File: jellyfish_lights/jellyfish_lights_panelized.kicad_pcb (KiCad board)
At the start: 2 copper layers, 162.8 x 143.6 mm, 424 parts, among them Q1 AO3400A, SW1 tilt switch, U1 SN74LVC1G14DBV

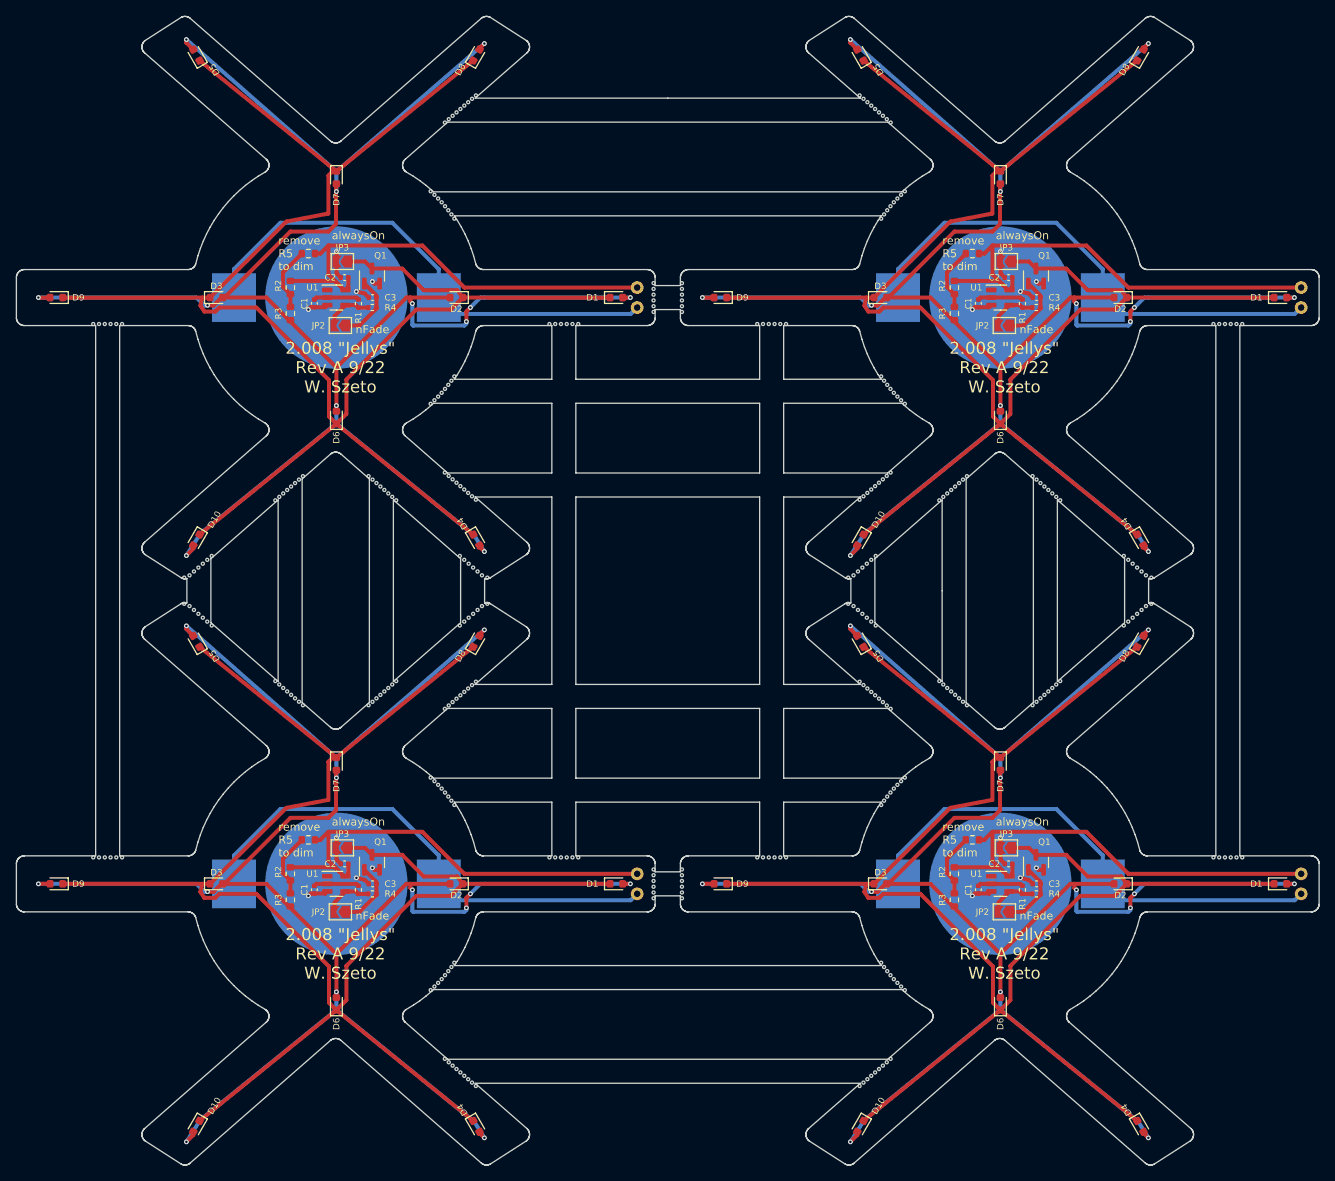
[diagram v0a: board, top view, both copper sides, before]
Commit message: Rev B01
Changed board shape
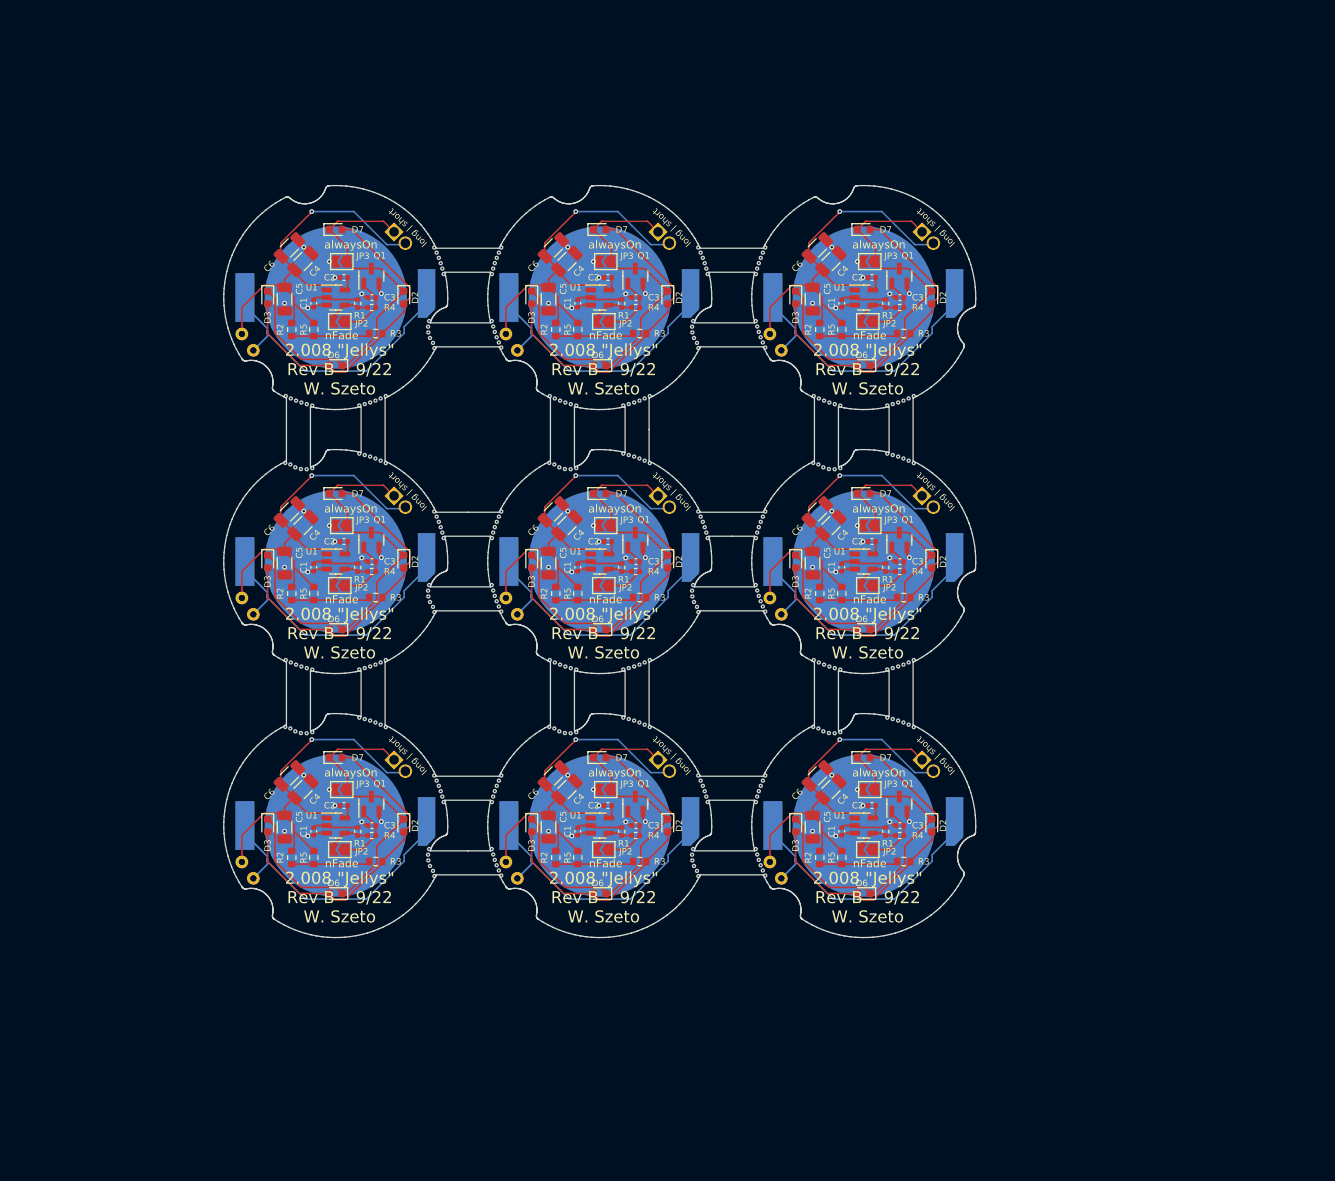
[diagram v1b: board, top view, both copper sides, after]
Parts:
- removed the BT1 at (50.1, 50.0)
- removed the BT1 at (133.1, 123.3)
- removed the BT1 at (133.1, 50.0)
- removed the BT1 at (50.1, 123.3)
- removed the C1 at (47.3, 50.7)
- removed the C1 at (130.3, 50.7)
- removed the C1 at (130.3, 124.0)
- removed the C1 at (47.3, 124.0)
- removed the C2 at (51.1, 120.8)
- removed the C2 at (134.1, 120.8)
- removed the C2 at (134.1, 47.5)
- removed the C2 at (51.1, 47.5)
- removed the C3 at (54.6, 50.0)
- removed the C3 at (137.6, 123.3)
- removed the C3 at (54.6, 123.3)
- removed the C3 at (137.6, 50.0)
- removed the D1 at (85.1, 123.3)
- removed the D1 at (168.1, 50.0)
- removed the D1 at (85.1, 50.0)
- removed the D1 at (168.1, 123.3)
- removed D10 (x4), D4 (x4), D5 (x4), D8 (x4), D9 (x4): LED, LED_SMD:LED_0603_1608Metric
- removed the D2 at (148.1, 50.0)
- removed the D2 at (65.1, 123.3)
- removed the D2 at (148.1, 123.3)
- removed the D2 at (65.1, 50.0)
- removed the D3 at (35.1, 50.0)
- removed the D3 at (118.1, 123.3)
- removed the D3 at (35.1, 123.3)
- removed the D3 at (118.1, 50.0)
- removed the D6 at (50.1, 138.3)
- removed the D6 at (133.1, 138.3)
- removed the D6 at (133.1, 65.0)
- removed the D6 at (50.1, 65.0)
- removed the D7 at (133.1, 108.3)
- removed the D7 at (50.1, 108.3)
- removed the D7 at (50.1, 35.0)
- removed the D7 at (133.1, 35.0)
- removed the JP2 at (50.6, 53.5)
- removed the JP2 at (50.6, 126.8)
- removed the JP2 at (133.6, 126.8)
- removed the JP2 at (133.6, 53.5)
- removed the JP3 at (50.8, 45.5)
- removed the JP3 at (50.8, 118.8)
- removed the JP3 at (133.8, 45.5)
- removed the JP3 at (133.8, 118.8)
- removed the Q1 at (137.5, 120.6)
- removed the Q1 at (137.5, 47.3)
- removed the Q1 at (54.5, 47.3)
- removed the Q1 at (54.5, 120.6)
- removed the R1 at (52.8, 50.7)
- removed the R1 at (135.8, 50.7)
- removed the R1 at (52.8, 124.0)
- removed the R1 at (135.8, 124.0)
- removed the R2 at (127.3, 122.0)
- removed the R2 at (127.3, 48.7)
- removed the R2 at (44.3, 122.0)
- removed the R2 at (44.3, 48.7)
- removed the R3 at (127.3, 52.0)
- removed the R3 at (44.3, 52.0)
- removed the R3 at (44.3, 125.3)
- removed the R3 at (127.3, 125.3)
- removed the R4 at (137.6, 124.5)
- removed the R4 at (54.6, 124.5)
- removed the R4 at (54.6, 51.2)
- removed the R4 at (137.6, 51.2)
- removed the R5 at (46.6, 44.5)
- removed the R5 at (129.6, 117.8)
- removed the R5 at (46.6, 117.8)
- removed the R5 at (129.6, 44.5)
- removed the REF** at (137.6, 72.8)
- removed the REF** at (128.9, 101.0)
- removed the REF** at (119.3, 111.9)
- removed the REF** at (121.1, 63.3)
- removed the REF** at (150.7, 84.2)
- removed the REF** at (66.6, 25.6)
- removed the REF** at (66.1, 26.0)
- removed the REF** at (118.4, 72.7)
- removed the REF** at (118.9, 72.3)
- removed the REF** at (148.5, 91.0)
- removed the REF** at (66.1, 147.3)
- removed the REF** at (119.3, 134.7)
- removed the REF** at (137.1, 72.3)
- removed the REF** at (138.1, 73.2)
- removed the REF** at (103.4, 53.3)
- removed the REF** at (63.2, 111.4)
- removed the REF** at (161.2, 53.3)
- removed the REF** at (93.3, 48.2)
- removed the REF** at (105.6, 53.3)
- removed the REF** at (56.1, 99.2)
- removed the REF** at (61.9, 36.7)
- removed the REF** at (65.1, 73.1)
- removed the REF** at (31.7, 84.7)
- removed the REF** at (56.6, 74.5)
- removed the REF** at (61.9, 110.0)
- removed the REF** at (62.3, 110.5)
- removed the REF** at (66.1, 99.3)
- removed the REF** at (43.4, 74.5)
- removed the REF** at (125.4, 75.3)
- removed the REF** at (126.9, 74.1)
- removed the REF** at (162.6, 53.3)
- removed the REF** at (45.9, 101.0)
- removed the REF** at (32.8, 89.5)
- removed the REF** at (117.9, 100.1)
- removed the REF** at (64.8, 40.1)
- removed the REF** at (103.4, 120.0)
- removed the REF** at (66.6, 90.0)
- removed the REF** at (119.4, 145.2)
- removed the REF** at (89.7, 122.9)
- removed the REF** at (119.8, 135.2)
- removed the REF** at (67.7, 84.2)
- removed the REF** at (148.5, 82.3)
- removed the REF** at (55.1, 100.1)
- removed the REF** at (116.9, 147.3)
- removed the REF** at (93.3, 121.5)
- removed the REF** at (64.6, 100.6)
- removed the REF** at (89.7, 49.6)
- removed the REF** at (116.4, 83.3)
- removed the REF** at (57.6, 75.3)
- removed the REF** at (128.4, 100.5)
- removed the REF** at (151.3, 84.7)
- removed the REF** at (64.5, 39.6)
- removed the REF** at (126.9, 99.2)
- removed the REF** at (65.1, 146.4)
- removed the REF** at (138.1, 100.1)
- removed the REF** at (61.9, 136.6)
- removed the REF** at (31.1, 88.3)
- removed the REF** at (64.1, 27.7)
- removed the REF** at (118.9, 145.6)
- removed the REF** at (137.6, 100.5)
- removed the REF** at (66.5, 98.9)
- removed the REF** at (63.2, 38.1)
- removed the REF** at (89.7, 125.1)
- removed the REF** at (64.1, 72.3)
- removed the REF** at (119.8, 61.9)
- removed the REF** at (65.6, 26.4)
- removed the REF** at (114.1, 88.3)
- removed the REF** at (63.7, 111.9)
- removed the REF** at (117.4, 146.9)
- removed the REF** at (43.4, 98.8)
- removed the REF** at (140.6, 97.9)
- removed the REF** at (89.7, 51.8)
- removed the REF** at (89.7, 51.1)
- removed the REF** at (55.6, 73.6)
- removed the REF** at (127.4, 73.6)
- removed the REF** at (118.5, 39.6)
- removed the REF** at (43.9, 99.2)
- removed the REF** at (149.1, 90.5)
- removed the REF** at (64.8, 133.1)
- removed the REF** at (106.3, 53.3)
- removed the REF** at (89.7, 48.9)
- removed the REF** at (45.4, 72.8)
- removed the REF** at (93.3, 51.8)
- removed the REF** at (163.3, 53.3)
- removed the REF** at (64.1, 134.2)
- removed the REF** at (119.8, 111.4)
- removed the REF** at (78.2, 53.3)
- removed the REF** at (116.9, 90.5)
- removed the REF** at (21.1, 53.3)
- removed the REF** at (161.2, 120.0)
- removed the REF** at (161.9, 53.3)
- removed the REF** at (120.2, 110.9)
- removed the REF** at (150.2, 89.5)
- removed the REF** at (64.1, 60.9)
- removed the REF** at (80.3, 120.0)
- removed the REF** at (62.8, 37.6)
- removed the REF** at (67.0, 98.4)
- removed the REF** at (118.4, 27.3)
- removed the REF** at (54.1, 72.3)
- removed the REF** at (151.9, 88.3)
- removed the REF** at (89.7, 50.4)
- removed the REF** at (117.5, 82.3)
- removed the REF** at (116.0, 74.8)
- removed the REF** at (44.9, 100.1)
- removed the REF** at (121.1, 110.0)
- removed the REF** at (43.9, 74.1)
- removed the REF** at (105.6, 120.0)
- removed the REF** at (67.5, 98.0)
- removed the REF** at (65.5, 82.3)
- removed the REF** at (64.1, 101.0)
- removed the REF** at (117.9, 26.9)
- removed the REF** at (80.3, 53.3)
- removed the REF** at (76.7, 120.0)
- removed the REF** at (159.7, 120.0)
- removed the REF** at (118.9, 101.0)
- removed the REF** at (159.7, 53.3)
- removed the REF** at (65.1, 26.9)
- removed the REF** at (162.6, 120.0)
- removed the REF** at (67.2, 89.5)
- removed the REF** at (63.7, 61.4)
- removed the REF** at (126.4, 98.8)
- removed the REF** at (139.1, 99.2)
- removed the REF** at (93.3, 125.1)
- removed the REF** at (21.8, 120.0)
- removed the REF** at (68.9, 85.0)
- removed the REF** at (93.3, 49.6)
- removed the REF** at (116.0, 148.1)
- removed the REF** at (119.4, 101.4)
- removed the REF** at (31.7, 88.6)
- removed the REF** at (116.9, 74.0)
- removed the REF** at (115.5, 75.3)
- removed the REF** at (42.4, 75.3)
- removed the REF** at (114.7, 84.7)
- removed the REF** at (118.9, 27.7)
- removed the REF** at (89.7, 121.5)
- removed the REF** at (44.4, 73.6)
- removed the REF** at (149.6, 83.3)
- removed the REF** at (63.6, 101.4)
- removed the REF** at (44.9, 73.2)
- removed the REF** at (118.2, 59.9)
- removed the REF** at (34.5, 91.0)
- removed the REF** at (67.5, 24.7)
- removed the REF** at (42.9, 98.4)
- removed the REF** at (161.9, 120.0)
- removed the REF** at (64.8, 113.4)
- removed the REF** at (63.7, 38.6)
- removed the REF** at (149.1, 82.8)
- removed the REF** at (54.6, 100.5)
- removed the REF** at (67.2, 83.8)
- removed the REF** at (55.6, 99.7)
- removed the REF** at (120.7, 37.2)
- removed the REF** at (21.8, 53.3)
- removed the REF** at (116.0, 25.2)
- removed the REF** at (137.1, 101.0)
- removed the REF** at (32.3, 89.1)
- removed the REF** at (140.1, 74.9)
- removed the REF** at (67.7, 89.1)
- removed the REF** at (115.8, 83.8)
- removed the REF** at (66.6, 83.3)
- removed the REF** at (76.7, 53.3)
- removed the REF** at (139.6, 74.5)
- removed the REF** at (114.7, 88.6)
- removed the REF** at (128.4, 72.8)
- removed the REF** at (120.7, 136.1)
- removed the REF** at (23.3, 120.0)
- removed the REF** at (57.1, 74.9)
- removed the REF** at (63.2, 61.9)
- removed the REF** at (33.4, 83.3)
- removed the REF** at (150.2, 83.8)
- removed the REF** at (139.1, 74.1)
- removed the REF** at (79.6, 120.0)
- removed the REF** at (68.3, 88.6)
- removed the REF** at (104.1, 53.3)
- removed the REF** at (33.4, 90.0)
- removed the REF** at (119.3, 38.6)
- removed the REF** at (117.9, 73.1)
- removed the REF** at (120.2, 37.6)
- removed the REF** at (22.6, 120.0)
- removed the REF** at (65.6, 146.9)
- removed the REF** at (34.5, 82.3)
- removed the REF** at (89.7, 122.2)
- removed the REF** at (117.4, 99.7)
- removed the REF** at (63.6, 28.1)
- removed the REF** at (45.9, 72.3)
- removed the REF** at (117.5, 91.0)
- removed the REF** at (33.9, 90.5)
- removed the REF** at (104.8, 53.3)
- removed the REF** at (64.1, 145.6)
- removed the REF** at (116.9, 82.8)
- removed the REF** at (138.6, 99.7)
- removed the REF** at (57.6, 97.9)
- removed the REF** at (127.4, 99.7)
- removed the REF** at (118.9, 60.9)
- removed the REF** at (66.5, 74.4)
- removed the REF** at (64.5, 133.7)
- removed the REF** at (65.1, 100.1)
- removed the REF** at (63.6, 145.2)
- removed the REF** at (140.1, 98.4)
- removed the REF** at (118.9, 39.1)
- removed the REF** at (89.7, 123.6)
- removed the REF** at (44.4, 99.7)
- removed the REF** at (31.1, 85.0)
- removed the REF** at (140.6, 75.3)
- removed the REF** at (118.9, 134.2)
- removed the REF** at (56.1, 74.1)
- removed the REF** at (77.4, 53.3)
- removed the REF** at (23.3, 53.3)
- removed the REF** at (115.5, 24.7)
- removed the REF** at (116.9, 26.0)
- removed the REF** at (118.4, 146.0)
- removed the REF** at (116.0, 98.4)
- removed the REF** at (89.7, 124.4)
- removed the REF** at (119.3, 61.4)
- removed the REF** at (104.8, 120.0)
- removed the REF** at (104.1, 120.0)
- removed the REF** at (119.4, 28.1)
- removed the REF** at (128.9, 72.3)
- removed the REF** at (116.5, 25.6)
- removed the REF** at (78.9, 120.0)
- removed the REF** at (114.1, 85.0)
- removed the REF** at (102.7, 53.3)
- removed the REF** at (68.9, 88.3)
- removed the REF** at (93.3, 124.4)
- removed the REF** at (163.3, 120.0)
- removed the REF** at (151.9, 85.0)
- removed the REF** at (118.2, 40.1)
- removed the REF** at (118.9, 112.4)
- removed the REF** at (120.2, 62.4)
- removed the REF** at (21.1, 120.0)
- removed the REF** at (116.9, 99.3)
- removed the REF** at (149.6, 90.0)
- removed the REF** at (125.9, 74.9)
- removed the REF** at (32.8, 83.8)
- removed the REF** at (63.7, 134.7)
- removed the REF** at (56.6, 98.8)
- removed the REF** at (151.3, 88.6)
- removed the REF** at (66.1, 82.8)
- removed the REF** at (117.4, 26.4)
- removed the REF** at (115.8, 89.5)
- removed the REF** at (117.4, 73.6)
- removed the REF** at (20.4, 53.3)
- removed the REF** at (150.7, 89.1)
- removed the REF** at (78.2, 120.0)
- removed the REF** at (66.1, 90.5)
- removed the REF** at (19.7, 53.3)
- removed the REF** at (119.8, 38.1)
- removed the REF** at (54.6, 72.8)
- removed the REF** at (66.1, 74.0)
- removed the REF** at (117.9, 146.4)
- removed the REF** at (115.3, 89.1)
- removed the REF** at (127.9, 100.1)
- removed the REF** at (54.1, 101.0)
- removed the REF** at (93.3, 123.6)
- removed the REF** at (93.3, 51.1)
- removed the REF** at (125.4, 97.9)
- removed the REF** at (160.4, 120.0)
- removed the REF** at (126.4, 74.5)
- removed the REF** at (67.0, 74.8)
- removed the REF** at (121.1, 36.7)
- removed the REF** at (120.7, 110.5)
- removed the REF** at (93.3, 122.9)
- removed the REF** at (116.4, 147.7)
- removed the REF** at (118.5, 112.9)
- removed the REF** at (64.8, 59.9)
- removed the REF** at (139.6, 98.8)
- removed the REF** at (19.7, 120.0)
- removed the REF** at (78.9, 53.3)
- removed the REF** at (118.2, 133.1)
- removed the REF** at (118.4, 100.6)
- removed the REF** at (115.5, 148.6)
- removed the REF** at (138.6, 73.6)
- removed the REF** at (22.6, 53.3)
- removed the REF** at (64.1, 112.4)
- removed the REF** at (116.5, 98.9)
- removed the REF** at (121.1, 136.6)
- removed the REF** at (64.6, 27.3)
- removed the REF** at (65.6, 99.7)
- removed the REF** at (115.5, 98.0)
- removed the REF** at (125.9, 98.4)
- removed the REF** at (93.3, 122.2)
- removed the REF** at (62.3, 37.2)
- removed the REF** at (120.7, 62.8)
- removed the REF** at (93.3, 50.4)
- removed the REF** at (65.5, 91.0)
- removed the REF** at (20.4, 120.0)
- removed the REF** at (63.2, 135.2)
- removed the REF** at (55.1, 73.2)
- removed the REF** at (77.4, 120.0)
- removed the REF** at (93.3, 48.9)
- removed the REF** at (64.1, 39.1)
- removed the REF** at (64.6, 72.7)
- removed the REF** at (127.9, 73.2)
- removed the REF** at (67.0, 25.2)
- removed the REF** at (62.3, 136.1)
- removed the REF** at (65.6, 73.6)
- removed the REF** at (45.4, 100.5)
- removed the REF** at (33.9, 82.8)
- removed the REF** at (64.5, 112.9)
- removed the REF** at (106.3, 120.0)
- removed the REF** at (57.1, 98.4)
- removed the REF** at (68.3, 84.7)
- removed the REF** at (118.5, 60.4)
- removed the REF** at (42.4, 97.9)
- removed the REF** at (79.6, 53.3)
- removed the REF** at (64.5, 60.4)
- removed the REF** at (67.5, 75.3)
- removed the REF** at (118.2, 113.4)
- removed the REF** at (67.0, 148.1)
- removed the REF** at (64.6, 146.0)
- removed the REF** at (160.4, 53.3)
- removed the REF** at (116.4, 74.4)
- removed the REF** at (62.8, 110.9)
- removed the REF** at (62.8, 135.7)
- removed the REF** at (89.7, 48.2)
- removed the REF** at (66.6, 147.7)
- removed the REF** at (61.9, 63.3)
- removed the REF** at (118.5, 133.7)
- removed the REF** at (63.6, 71.9)
- removed the REF** at (116.4, 90.0)
- removed the REF** at (120.2, 135.7)
- removed the REF** at (67.5, 148.6)
- removed the REF** at (119.4, 71.9)
- removed the REF** at (32.3, 84.2)
- removed the REF** at (115.3, 84.2)
- removed the REF** at (62.8, 62.4)
- removed the REF** at (62.3, 62.8)
- removed the REF** at (42.9, 74.9)
- removed the REF** at (102.7, 120.0)
- removed the SW1 at (87.7, 122.0)
- removed the SW1 at (87.7, 48.7)
- removed the SW1 at (170.7, 48.7)
- removed the SW1 at (170.7, 122.0)
- removed the U1 at (133.1, 50.0)
- removed the U1 at (133.1, 123.3)
- removed the U1 at (50.1, 50.0)
- removed the U1 at (50.1, 123.3)
- added BT1: Battery_Cell, Battery:BatteryHolder_Keystone_3002_1x2032, B.Cu at (116.0, 83.0)
- added BT1: Battery_Cell, Battery:BatteryHolder_Keystone_3002_1x2032, B.Cu at (83.0, 50.0)
- added BT1: Battery_Cell, Battery:BatteryHolder_Keystone_3002_1x2032, B.Cu at (83.0, 83.0)
- added BT1: Battery_Cell, Battery:BatteryHolder_Keystone_3002_1x2032, B.Cu at (83.0, 116.0)
- added BT1: Battery_Cell, Battery:BatteryHolder_Keystone_3002_1x2032, B.Cu at (50.0, 116.0)
- added BT1: Battery_Cell, Battery:BatteryHolder_Keystone_3002_1x2032, B.Cu at (50.0, 83.0)
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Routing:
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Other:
- board size 162.8 x 143.6 mm -> 94 x 94 mm
- board text added: "2.008 {dblquote}Jellys{dblquote} Rev B 9/22 W. Szeto"
- board text added: "long"
- board text added: "long | short"
- board text added: "short"
- board text removed: "2.008 {dblquote}Jellys{dblquote} Rev A 9/22 W. Szeto"
- board text removed: "remove R5 to dim"

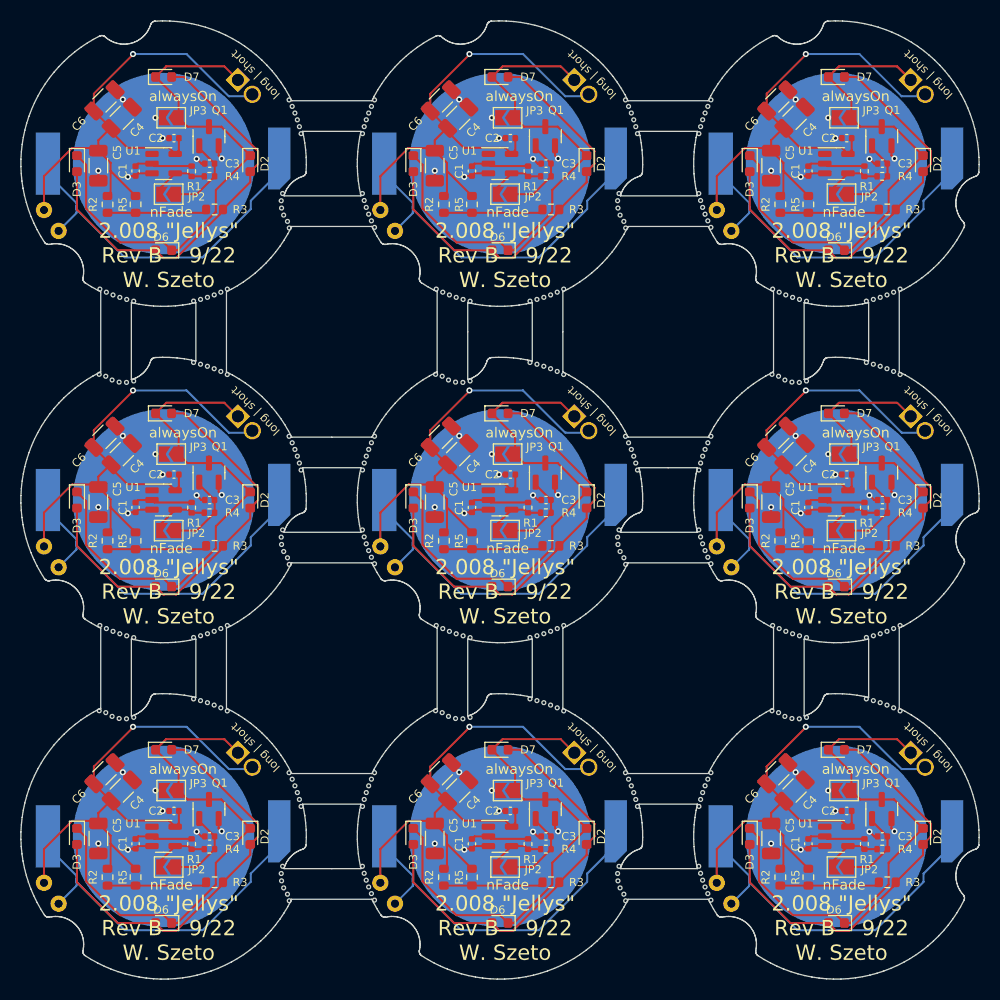
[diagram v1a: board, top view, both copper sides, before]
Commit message: Rev C01
-Edited THT footprints to accommodate easier soldering (moved away from BT1)
-Added SW2 to prevent turn-on events while not spinning
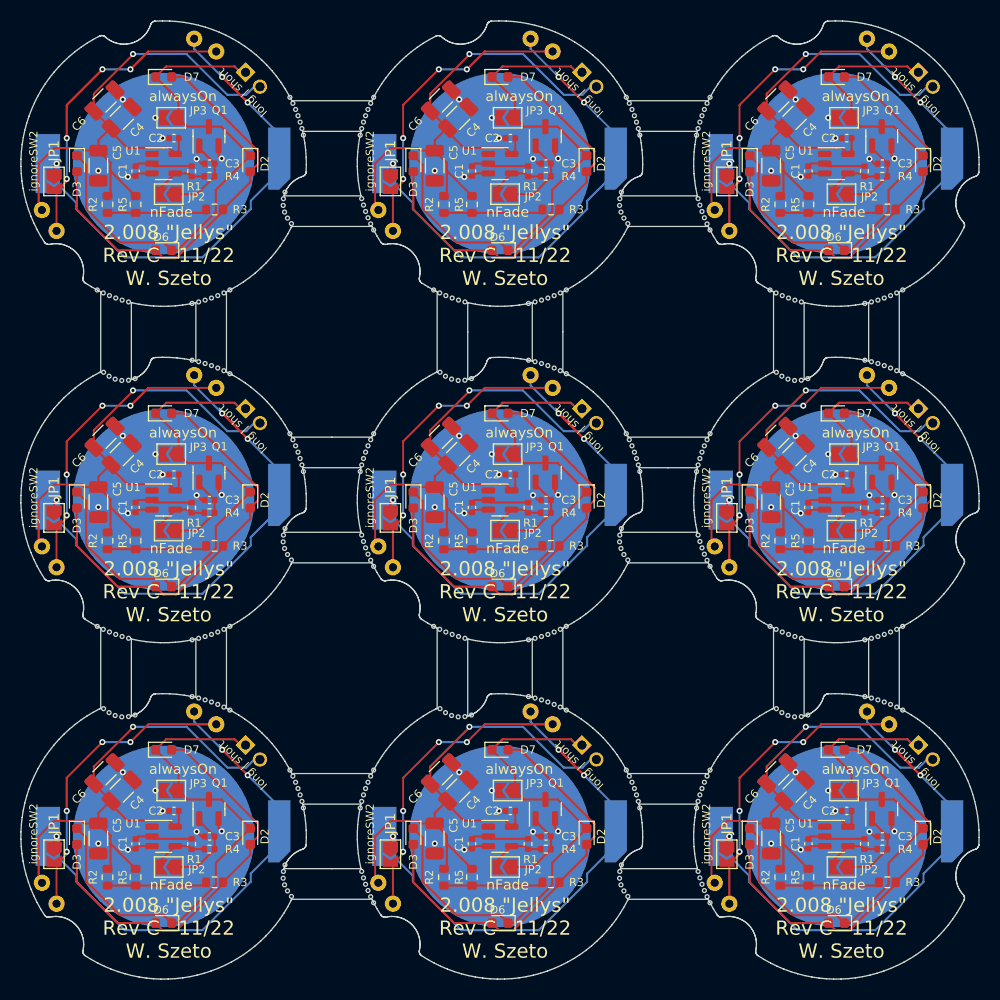
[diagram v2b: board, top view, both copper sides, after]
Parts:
- removed the D1 at (90.1, 41.6)
- removed the D1 at (90.1, 74.6)
- removed the D1 at (57.1, 107.6)
- removed the D1 at (123.1, 74.6)
- removed the D1 at (123.1, 41.6)
- removed the D1 at (57.1, 74.6)
- removed the D1 at (57.1, 41.6)
- removed the D1 at (90.1, 107.6)
- removed the D1 at (123.1, 107.6)
- removed the REF** at (78.7, 96.1)
- removed the REF** at (70.1, 45.0)
- removed the REF** at (122.2, 103.7)
- removed the REF** at (103.1, 111.0)
- removed the REF** at (94.8, 55.1)
- removed the REF** at (95.3, 122.3)
- removed the REF** at (118.9, 102.5)
- removed the REF** at (95.3, 43.8)
- removed the REF** at (113.1, 63.5)
- removed the REF** at (69.5, 118.9)
- removed the REF** at (70.1, 121.0)
- removed the REF** at (55.0, 70.1)
- removed the REF** at (94.5, 119.6)
- removed the REF** at (121.6, 70.4)
- removed the REF** at (56.2, 70.7)
- removed the REF** at (55.6, 70.4)
- removed the REF** at (102.7, 53.6)
- removed the REF** at (46.4, 96.3)
- removed the REF** at (78.0, 95.9)
- removed the REF** at (112.4, 96.3)
- removed the REF** at (62.3, 109.8)
- removed the REF** at (77.3, 70.9)
- removed the REF** at (95.2, 88.7)
- removed the REF** at (109.7, 103.7)
- removed the REF** at (44.3, 103.9)
- removed the REF** at (94.7, 52.9)
- removed the REF** at (78.6, 71.4)
- removed the REF** at (69.5, 85.9)
- removed the REF** at (80.1, 63.5)
- removed the REF** at (61.8, 88.1)
- removed the REF** at (96.3, 46.4)
- removed the REF** at (119.6, 69.7)
- removed the REF** at (62.2, 121.7)
- removed the REF** at (43.7, 62.3)
- removed the REF** at (103.1, 45.0)
- removed the REF** at (87.3, 63.1)
- removed the REF** at (86.6, 63.3)
- removed the REF** at (95.9, 78.0)
- removed the REF** at (85.9, 63.5)
- removed the REF** at (109.7, 70.7)
- removed the REF** at (88.6, 70.4)
- removed the REF** at (110.9, 104.2)
- removed the REF** at (44.3, 70.9)
- removed the REF** at (102.9, 120.3)
- removed the REF** at (69.5, 47.1)
- removed the REF** at (70.4, 121.6)
- removed the REF** at (111.7, 96.1)
- removed the REF** at (87.3, 102.9)
- removed the REF** at (61.8, 55.1)
- removed the REF** at (77.4, 62.6)
- removed the REF** at (96.5, 113.1)
- removed the REF** at (62.3, 56.3)
- removed the REF** at (112.4, 104.5)
- removed the REF** at (79.4, 63.3)
- removed the REF** at (94.7, 85.9)
- removed the REF** at (55.0, 103.1)
- removed the REF** at (69.7, 53.6)
- removed the REF** at (70.7, 43.7)
- removed the REF** at (102.9, 54.3)
- removed the REF** at (69.5, 113.1)
- removed the REF** at (70.7, 109.7)
- removed the REF** at (88.6, 95.6)
- removed the REF** at (45.0, 95.9)
- removed the REF** at (55.6, 95.6)
- removed the REF** at (43.7, 103.7)
- removed the REF** at (62.2, 55.7)
- removed the REF** at (86.6, 69.7)
- removed the REF** at (102.7, 79.4)
- removed the REF** at (79.4, 71.5)
- removed the REF** at (70.1, 78.0)
- removed the REF** at (43.7, 95.3)
- removed the REF** at (122.2, 70.7)
- removed the REF** at (102.5, 85.9)
- removed the REF** at (43.7, 70.7)
- removed the REF** at (94.7, 118.9)
- removed the REF** at (103.1, 88.0)
- removed the REF** at (95.2, 55.7)
- removed the REF** at (103.1, 78.0)
- removed the REF** at (62.3, 89.3)
- removed the REF** at (89.2, 70.7)
- removed the REF** at (119.6, 96.3)
- removed the REF** at (95.6, 77.4)
- removed the REF** at (89.2, 103.7)
- removed the REF** at (54.3, 69.9)
- removed the REF** at (102.7, 112.4)
- removed the REF** at (69.7, 46.4)
- removed the REF** at (61.5, 119.6)
- removed the REF** at (85.9, 96.5)
- removed the REF** at (112.4, 71.5)
- removed the REF** at (61.5, 53.6)
- removed the REF** at (111.6, 71.4)
- removed the REF** at (61.6, 54.4)
- removed the REF** at (121.0, 103.1)
- removed the REF** at (95.9, 111.0)
- removed the REF** at (95.3, 76.8)
- removed the REF** at (110.9, 71.2)
- removed the REF** at (95.3, 89.3)
- removed the REF** at (121.6, 95.6)
- removed the REF** at (103.7, 109.7)
- removed the REF** at (103.1, 121.0)
- removed the REF** at (54.3, 102.9)
- removed the REF** at (61.6, 87.4)
- removed the REF** at (76.7, 95.3)
- removed the REF** at (103.7, 76.7)
- removed the REF** at (62.9, 111.0)
- removed the REF** at (88.6, 62.6)
- removed the REF** at (95.2, 121.7)
- removed the REF** at (89.3, 62.3)
- removed the REF** at (69.5, 52.9)
- removed the REF** at (94.5, 53.6)
- removed the REF** at (88.0, 62.9)
- removed the REF** at (69.9, 111.7)
- removed the REF** at (45.7, 96.1)
- removed the REF** at (52.9, 69.5)
- removed the REF** at (120.3, 102.9)
- removed the REF** at (62.9, 78.0)
- removed the REF** at (63.3, 79.4)
- removed the REF** at (111.6, 104.4)
- removed the REF** at (110.3, 103.9)
- removed the REF** at (45.6, 71.4)
- removed the REF** at (44.9, 71.2)
- removed the REF** at (69.7, 119.6)
- removed the REF** at (69.9, 87.3)
- removed the REF** at (118.9, 63.5)
- removed the REF** at (52.9, 102.5)
- removed the REF** at (113.1, 104.3)
- removed the REF** at (109.7, 95.3)
- removed the REF** at (62.3, 122.3)
- removed the REF** at (95.6, 44.4)
- removed the REF** at (94.5, 86.6)
- removed the REF** at (119.6, 102.7)
- removed the REF** at (120.3, 69.9)
- removed the REF** at (109.7, 62.3)
- removed the REF** at (45.7, 63.1)
- removed the REF** at (76.7, 103.7)
- removed the REF** at (102.9, 87.3)
- removed the REF** at (111.0, 62.9)
- removed the REF** at (62.6, 110.4)
- removed the REF** at (87.3, 69.9)
- removed the REF** at (111.7, 63.1)
- removed the REF** at (103.4, 110.4)
- removed the REF** at (94.6, 120.4)
- removed the REF** at (94.6, 54.4)
- removed the REF** at (89.3, 95.3)
- removed the REF** at (62.2, 88.7)
- removed the REF** at (61.7, 52.9)
- removed the REF** at (62.3, 76.8)
- removed the REF** at (88.0, 70.1)
- removed the REF** at (55.6, 62.6)
- removed the REF** at (47.1, 71.3)
- removed the REF** at (103.7, 122.3)
- removed the REF** at (70.4, 110.4)
- removed the REF** at (56.3, 95.3)
- removed the REF** at (63.1, 111.7)
- removed the REF** at (88.0, 95.9)
- removed the REF** at (103.4, 55.6)
- removed the REF** at (77.9, 71.2)
- removed the REF** at (44.4, 95.6)
- removed the REF** at (46.4, 71.5)
- removed the REF** at (120.3, 63.1)
- removed the REF** at (61.7, 85.9)
- removed the REF** at (121.0, 62.9)
- removed the REF** at (55.0, 95.9)
- removed the REF** at (47.1, 63.5)
- removed the REF** at (47.1, 104.3)
- removed the REF** at (70.4, 44.4)
- removed the REF** at (102.7, 46.4)
- removed the REF** at (69.9, 78.7)
- removed the REF** at (112.4, 63.3)
- removed the REF** at (103.7, 89.3)
- removed the REF** at (69.7, 86.6)
- removed the REF** at (111.0, 95.9)
- removed the REF** at (61.8, 121.1)
- removed the REF** at (70.4, 55.6)
- removed the REF** at (102.7, 119.6)
- removed the REF** at (94.6, 87.4)
- removed the REF** at (69.9, 54.3)
- removed the REF** at (80.1, 96.5)
- removed the REF** at (121.6, 103.4)
- removed the REF** at (61.6, 120.4)
- removed the REF** at (102.5, 47.1)
- removed the REF** at (63.5, 113.1)
- removed the REF** at (76.7, 70.7)
- removed the REF** at (76.7, 62.3)
- removed the REF** at (78.0, 62.9)
- removed the REF** at (69.9, 120.3)
- removed the REF** at (53.6, 69.7)
- removed the REF** at (78.7, 63.1)
- removed the REF** at (95.3, 109.8)
- removed the REF** at (102.9, 78.7)
- removed the REF** at (103.4, 88.6)
- removed the REF** at (110.4, 62.6)
- removed the REF** at (102.5, 80.1)
- removed the REF** at (70.1, 55.0)
- removed the REF** at (52.9, 63.5)
- removed the REF** at (56.3, 62.3)
- removed the REF** at (77.4, 95.6)
- removed the REF** at (63.5, 80.1)
- removed the REF** at (55.0, 62.9)
- removed the REF** at (86.6, 96.3)
- removed the REF** at (54.3, 63.1)
- removed the REF** at (94.8, 121.1)
- removed the REF** at (102.5, 113.1)
- removed the REF** at (78.6, 104.4)
- removed the REF** at (53.6, 63.3)
- removed the REF** at (94.8, 88.1)
- removed the REF** at (103.7, 56.3)
- removed the REF** at (119.6, 63.3)
- removed the REF** at (118.9, 69.5)
- removed the REF** at (103.4, 121.6)
- removed the REF** at (53.6, 96.3)
- removed the REF** at (56.2, 103.7)
- removed the REF** at (103.4, 44.4)
- removed the REF** at (63.1, 45.7)
- removed the REF** at (63.5, 47.1)
- removed the REF** at (70.4, 88.6)
- removed the REF** at (45.6, 104.4)
- removed the REF** at (46.4, 63.3)
- removed the REF** at (121.0, 70.1)
- removed the REF** at (70.7, 122.3)
- removed the REF** at (47.1, 96.5)
- removed the REF** at (87.3, 96.1)
- removed the REF** at (110.4, 95.6)
- removed the REF** at (62.3, 43.8)
- removed the REF** at (96.3, 79.4)
- removed the REF** at (110.3, 70.9)
- removed the REF** at (69.7, 112.4)
- removed the REF** at (103.7, 43.7)
- removed the REF** at (95.9, 45.0)
- removed the REF** at (45.0, 62.9)
- removed the REF** at (102.9, 111.7)
- removed the REF** at (121.0, 95.9)
- removed the REF** at (55.6, 103.4)
- removed the REF** at (102.5, 52.9)
- removed the REF** at (103.4, 77.4)
- removed the REF** at (88.0, 103.1)
- removed the REF** at (95.3, 56.3)
- removed the REF** at (79.4, 96.3)
- removed the REF** at (102.9, 45.7)
- removed the REF** at (85.9, 69.5)
- removed the REF** at (96.1, 45.7)
- removed the REF** at (61.7, 118.9)
- removed the REF** at (69.5, 80.1)
- removed the REF** at (120.3, 96.1)
- removed the REF** at (80.1, 104.3)
- removed the REF** at (77.9, 104.2)
- removed the REF** at (121.6, 62.6)
- removed the REF** at (70.7, 56.3)
- removed the REF** at (85.9, 102.5)
- removed the REF** at (80.1, 71.3)
- removed the REF** at (61.5, 86.6)
- removed the REF** at (102.7, 86.6)
- removed the REF** at (62.6, 44.4)
- removed the REF** at (79.4, 104.5)
- removed the REF** at (63.1, 78.7)
- removed the REF** at (70.1, 111.0)
- removed the REF** at (70.4, 77.4)
- removed the REF** at (54.3, 96.1)
- removed the REF** at (103.1, 55.0)
- removed the REF** at (63.3, 46.4)
- removed the REF** at (52.9, 96.5)
- removed the REF** at (96.1, 78.7)
- removed the REF** at (96.5, 47.1)
- removed the REF** at (44.4, 62.6)
- removed the REF** at (70.1, 88.0)
- removed the REF** at (88.6, 103.4)
- removed the REF** at (96.5, 80.1)
- removed the REF** at (113.1, 96.5)
- removed the REF** at (53.6, 102.7)
- removed the REF** at (62.6, 77.4)
- removed the REF** at (122.3, 62.3)
- removed the REF** at (69.7, 79.4)
- removed the REF** at (113.1, 71.3)
- removed the REF** at (95.6, 110.4)
- removed the REF** at (102.5, 118.9)
- removed the REF** at (118.9, 96.5)
- removed the REF** at (44.9, 104.2)
- removed the REF** at (122.3, 95.3)
- removed the REF** at (62.9, 45.0)
- removed the REF** at (77.3, 103.9)
- removed the REF** at (63.3, 112.4)
- removed the REF** at (96.1, 111.7)
- removed the REF** at (96.3, 112.4)
- removed the REF** at (70.7, 89.3)
- removed the REF** at (70.7, 76.7)
- removed the REF** at (86.6, 102.7)
- removed the REF** at (46.4, 104.5)
- removed the REF** at (69.9, 45.7)
- removed the SW1 at (105.7, 56.6)
- removed the SW1 at (39.7, 122.6)
- removed the SW1 at (72.7, 122.6)
- removed the SW1 at (72.7, 56.6)
- removed the SW1 at (105.7, 89.6)
- removed the SW1 at (39.7, 56.6)
- removed the SW1 at (39.7, 89.6)
- removed the SW1 at (105.7, 122.6)
- removed the SW1 at (72.7, 89.6)
- added D1: 3mm THT LED, LED_THT:LED_D5.0mm_FlatTop, B.Cu at (90.8, 106.8)
- added D1: 3mm THT LED, LED_THT:LED_D5.0mm_FlatTop, B.Cu at (90.8, 40.8)
- added D1: 3mm THT LED, LED_THT:LED_D5.0mm_FlatTop, B.Cu at (123.8, 106.8)
- added D1: 3mm THT LED, LED_THT:LED_D5.0mm_FlatTop, B.Cu at (57.8, 73.8)
- added D1: 3mm THT LED, LED_THT:LED_D5.0mm_FlatTop, B.Cu at (90.8, 73.8)
- added D1: 3mm THT LED, LED_THT:LED_D5.0mm_FlatTop, B.Cu at (123.8, 40.8)
- added D1: 3mm THT LED, LED_THT:LED_D5.0mm_FlatTop, B.Cu at (123.8, 73.8)
- added D1: 3mm THT LED, LED_THT:LED_D5.0mm_FlatTop, B.Cu at (57.8, 106.8)
- added D1: 3mm THT LED, LED_THT:LED_D5.0mm_FlatTop, B.Cu at (57.8, 40.8)
- added JP1: oneTiltSw, Jumper:SolderJumper-2_P1.3mm_Open_TrianglePad1.0x1.5mm, F.Cu at (105.3, 117.8)
- added JP1: oneTiltSw, Jumper:SolderJumper-2_P1.3mm_Open_TrianglePad1.0x1.5mm, F.Cu at (39.2, 117.8)
- added JP1: oneTiltSw, Jumper:SolderJumper-2_P1.3mm_Open_TrianglePad1.0x1.5mm, F.Cu at (72.3, 117.8)
- added JP1: oneTiltSw, Jumper:SolderJumper-2_P1.3mm_Open_TrianglePad1.0x1.5mm, F.Cu at (39.2, 84.8)
- added JP1: oneTiltSw, Jumper:SolderJumper-2_P1.3mm_Open_TrianglePad1.0x1.5mm, F.Cu at (105.3, 84.8)
- added JP1: oneTiltSw, Jumper:SolderJumper-2_P1.3mm_Open_TrianglePad1.0x1.5mm, F.Cu at (105.3, 51.7)
- added JP1: oneTiltSw, Jumper:SolderJumper-2_P1.3mm_Open_TrianglePad1.0x1.5mm, F.Cu at (72.3, 84.8)
- added JP1: oneTiltSw, Jumper:SolderJumper-2_P1.3mm_Open_TrianglePad1.0x1.5mm, F.Cu at (72.3, 51.7)
- added JP1: oneTiltSw, Jumper:SolderJumper-2_P1.3mm_Open_TrianglePad1.0x1.5mm, F.Cu at (39.2, 51.7)
- added REF**: NPTH, NPTH, F.Cu at (70.3, 121.9)
- added REF**: NPTH, NPTH, F.Cu at (70.3, 110.1)
- added REF**: NPTH, NPTH, F.Cu at (44.7, 70.9)
- added REF**: NPTH, NPTH, F.Cu at (120.7, 102.8)
- added REF**: NPTH, NPTH, F.Cu at (118.8, 63.7)
- added REF**: NPTH, NPTH, F.Cu at (121.3, 63.0)
- added REF**: NPTH, NPTH, F.Cu at (94.9, 85.8)
- added REF**: NPTH, NPTH, F.Cu at (62.7, 44.1)
- added REF**: NPTH, NPTH, F.Cu at (94.7, 87.1)
- added REF**: NPTH, NPTH, F.Cu at (121.9, 70.3)
- added REF**: NPTH, NPTH, F.Cu at (78.9, 71.3)
- added REF**: NPTH, NPTH, F.Cu at (86.4, 102.4)
- added REF**: NPTH, NPTH, F.Cu at (103.6, 56.5)
- added REF**: NPTH, NPTH, F.Cu at (95.9, 110.7)
- added REF**: NPTH, NPTH, F.Cu at (79.6, 71.2)
- added REF**: NPTH, NPTH, F.Cu at (54.7, 102.8)
- added REF**: NPTH, NPTH, F.Cu at (111.2, 104.1)
- added REF**: NPTH, NPTH, F.Cu at (88.3, 63.0)
- added REF**: NPTH, NPTH, F.Cu at (61.7, 120.1)
- added REF**: NPTH, NPTH, F.Cu at (70.3, 44.1)
- added REF**: NPTH, NPTH, F.Cu at (62.2, 88.3)
- added REF**: NPTH, NPTH, F.Cu at (102.3, 113.2)
- added REF**: NPTH, NPTH, F.Cu at (103.0, 110.7)
- added REF**: NPTH, NPTH, F.Cu at (103.3, 88.9)
- added REF**: NPTH, NPTH, F.Cu at (43.5, 62.4)
- added REF**: NPTH, NPTH, F.Cu at (87.1, 102.6)
- added REF**: NPTH, NPTH, F.Cu at (79.6, 104.2)
- added REF**: NPTH, NPTH, F.Cu at (44.1, 70.5)
- added REF**: NPTH, NPTH, F.Cu at (63.6, 79.6)
- added REF**: NPTH, NPTH, F.Cu at (118.8, 69.3)
- added REF**: NPTH, NPTH, F.Cu at (96.2, 78.3)
- added REF**: NPTH, NPTH, F.Cu at (45.9, 96.4)
- added REF**: NPTH, NPTH, F.Cu at (110.7, 95.9)
- added REF**: NPTH, NPTH, F.Cu at (95.5, 55.9)
- added REF**: NPTH, NPTH, F.Cu at (55.3, 70.1)
- added REF**: NPTH, NPTH, F.Cu at (102.4, 46.6)
- added REF**: NPTH, NPTH, F.Cu at (121.9, 62.7)
- added REF**: NPTH, NPTH, F.Cu at (102.3, 47.2)
- added REF**: NPTH, NPTH, F.Cu at (54.1, 63.4)
- added REF**: NPTH, NPTH, F.Cu at (88.9, 103.3)
- added REF**: NPTH, NPTH, F.Cu at (70.3, 55.9)
- added REF**: NPTH, NPTH, F.Cu at (95.2, 121.3)
- added REF**: NPTH, NPTH, F.Cu at (78.2, 71.1)
- added REF**: NPTH, NPTH, F.Cu at (52.8, 63.7)
- added REF**: NPTH, NPTH, F.Cu at (103.6, 76.5)
- added REF**: NPTH, NPTH, F.Cu at (45.3, 63.2)
- added REF**: NPTH, NPTH, F.Cu at (70.3, 88.9)
- added REF**: NPTH, NPTH, F.Cu at (69.4, 79.6)
- added REF**: NPTH, NPTH, F.Cu at (94.9, 52.8)
- added REF**: NPTH, NPTH, F.Cu at (95.5, 88.9)
- added REF**: NPTH, NPTH, F.Cu at (77.1, 95.7)
- added REF**: NPTH, NPTH, F.Cu at (70.0, 44.7)
- added REF**: NPTH, NPTH, F.Cu at (56.5, 70.6)
- added REF**: NPTH, NPTH, F.Cu at (55.9, 70.3)
- added REF**: NPTH, NPTH, F.Cu at (94.8, 86.4)
- added REF**: NPTH, NPTH, F.Cu at (96.4, 78.9)
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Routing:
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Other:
- board text added: "2.008 {dblquote}Jellys{dblquote} Rev C 11/22 W. Szeto"
- board text added: "ignoreSW2"
- board text removed: "2.008 {dblquote}Jellys{dblquote} Rev B 9/22 W. Szeto"
- board text removed: "short"
